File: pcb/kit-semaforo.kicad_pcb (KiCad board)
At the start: 2 copper layers, 16 x 80 mm, 12 parts, among them P1 CONN_02X04

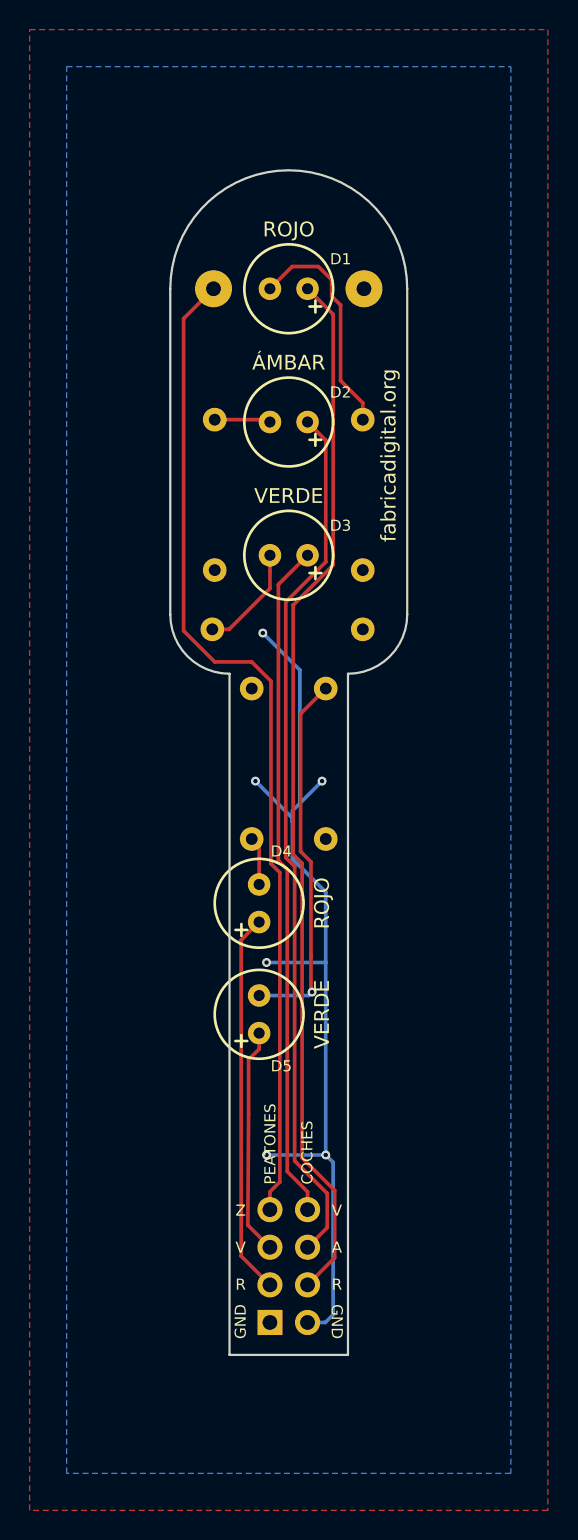
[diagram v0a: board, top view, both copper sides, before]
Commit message: Fix: tamaño huella zumbador. Nuevo: Pie ancho.
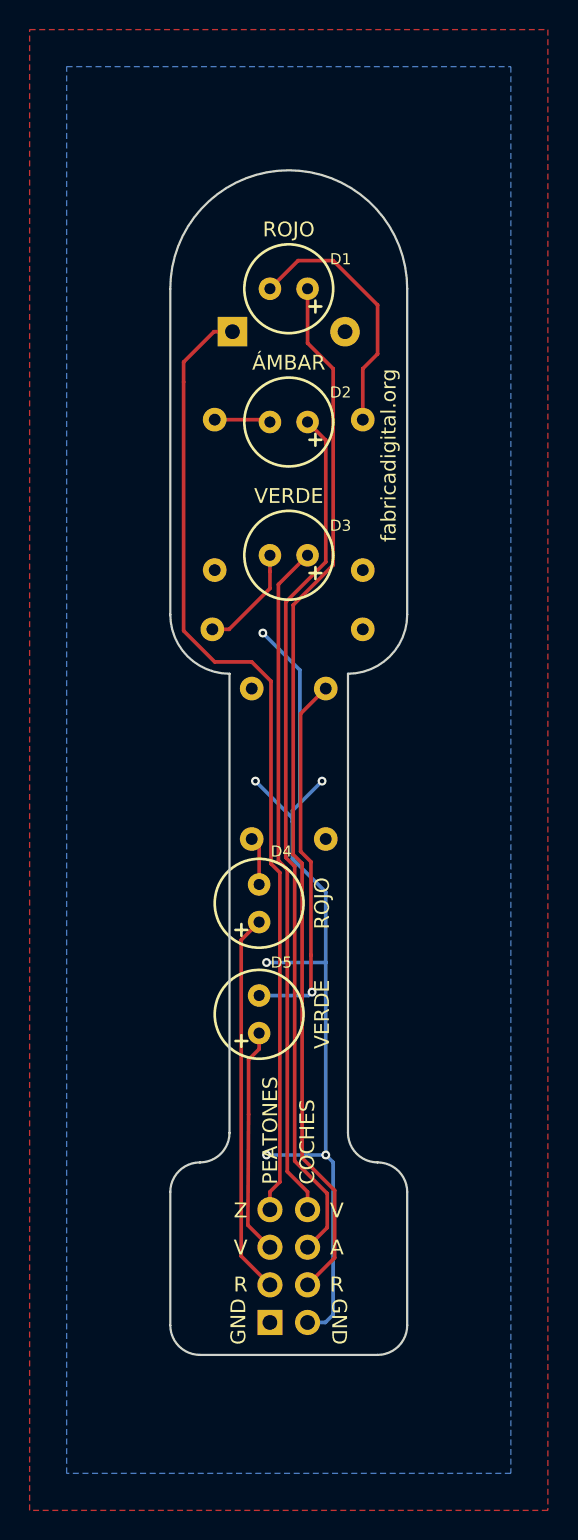
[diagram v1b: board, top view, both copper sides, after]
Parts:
- BZ1: footprint Buzzers_Beepers:BUZZER -> Buzzers_Beepers:Buzzer_12x9.5RM7.6
- moved BZ1 4.78 mm to (156.2, 82.9)
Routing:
- net Net-(D1-Pad1): track 15.5 -> 17.5 mm
- net /ZUMBADOR: track 67.5 -> 65.8 mm
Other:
- outline, holes or cut-outs redrawn

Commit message: v0.2a
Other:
- board text added: "v0.2a"
- board text removed: "v0.1a"

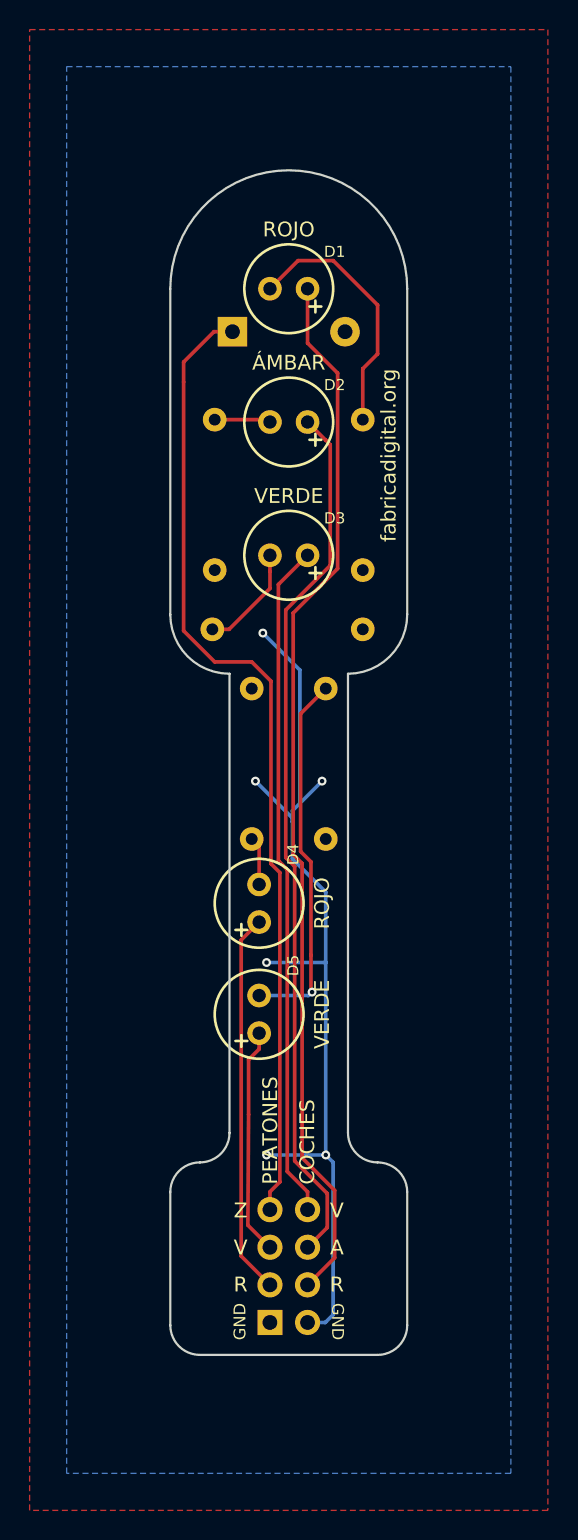
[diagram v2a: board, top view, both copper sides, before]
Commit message: 0.3a Añadido botón para peatones
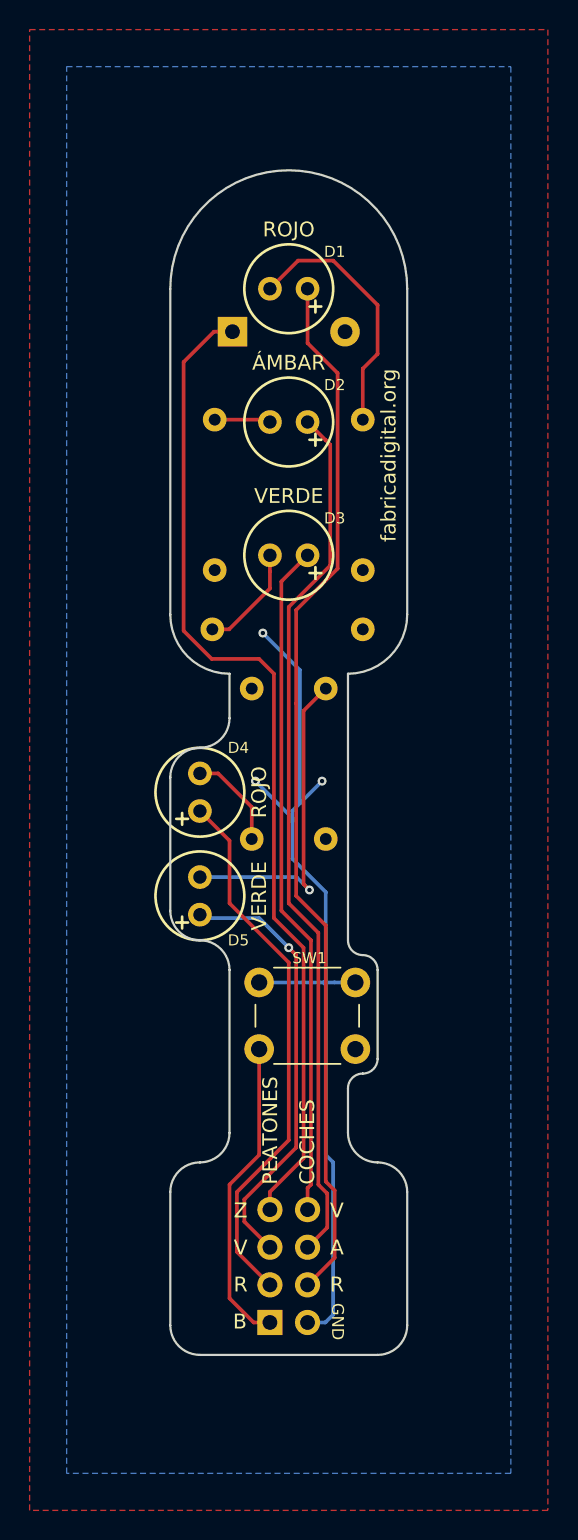
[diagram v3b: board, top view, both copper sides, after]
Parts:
- added SW1: Jumper, Buttons_Switches_THT:SW_PUSH_6mm, F.Cu at (164.5, 131.3)
- moved D5 8.94 mm to (154.0, 121.0)
- moved D4 8.50 mm to (154.0, 114.0)
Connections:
- P1 pad 1: GNDREF -> /BOTON
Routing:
- net /BOTON: track 0.00 -> 21.1 mm
- net /PEATONES-VERDE: track 15.4 -> 29.5 mm, vias 0 -> 1
- net /PEATONES-ROJO: track 25.8 -> 36.9 mm
- net Net-(D4-Pad1): track 3.28 -> 7.31 mm
- net Net-(D5-Pad1): track 25.2 -> 22.1 mm
- net /ZUMBADOR: track 65.8 -> 67.6 mm
- net GNDREF: track 64.3 -> 63.0 mm, vias 6 -> 3
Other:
- outline, holes or cut-outs redrawn
- board text added: "B"
- board text added: "v0.3a"
- board text removed: "v0.2a"
